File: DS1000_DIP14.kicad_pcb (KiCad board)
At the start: 2 copper layers, 8.9 x 16.5 mm, 3 parts, among them J1 DS1000, U2 DS1100Z

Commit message: kicad 6
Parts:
- U1: renamed from U2; value DS1100Z -> DS1100
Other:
- net class Default removed

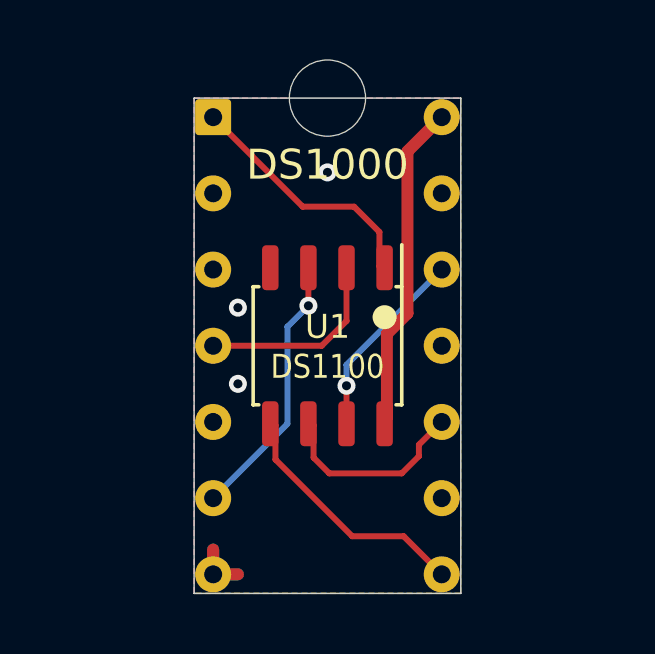
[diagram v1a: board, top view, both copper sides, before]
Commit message: Fix wrong pinout on FlashROM_100 TSOPgit add -A!
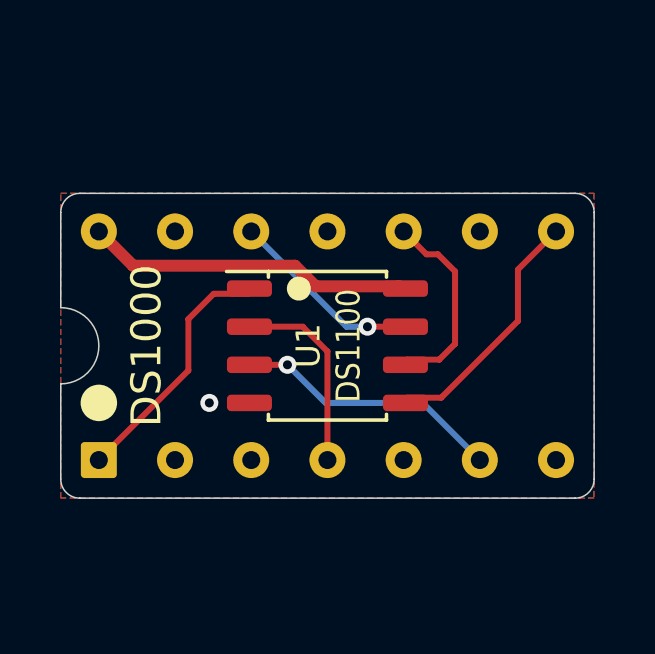
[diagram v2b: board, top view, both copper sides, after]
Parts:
- removed REF**: NPTH_0.1, 000_LOCAL:NPTH_0.1
- turned J1 to 90 degrees
- turned U1 to 0 degrees
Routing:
- net GND: track 3.30 -> 0.00 mm, vias 3 -> 1
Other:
- board size 8.9 x 16.5 mm -> 17.8 x 10.2 mm

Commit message: add SM8 DIP8, readme
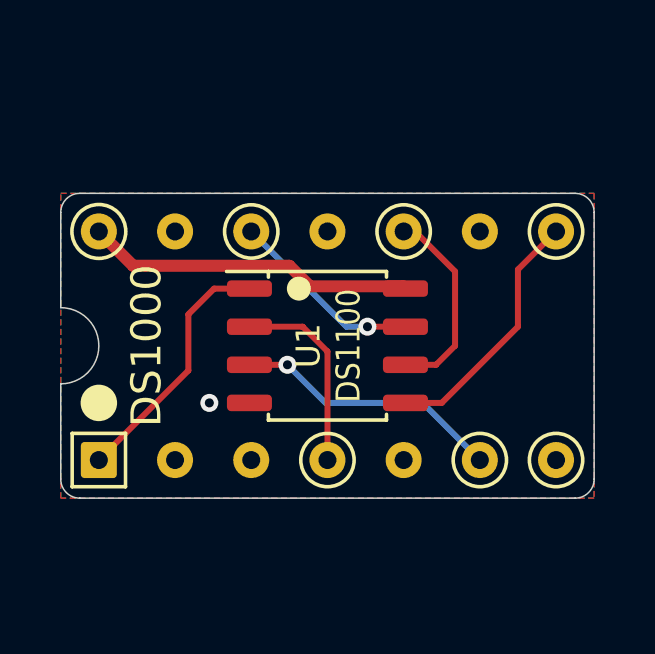
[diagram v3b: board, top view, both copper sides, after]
